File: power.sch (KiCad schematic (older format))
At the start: 33 parts, among them J2 4DB-P108-06, J3 39531-1002, J4 39531-1002, U2 i3A, U3 AP2112K-3.3TRG1

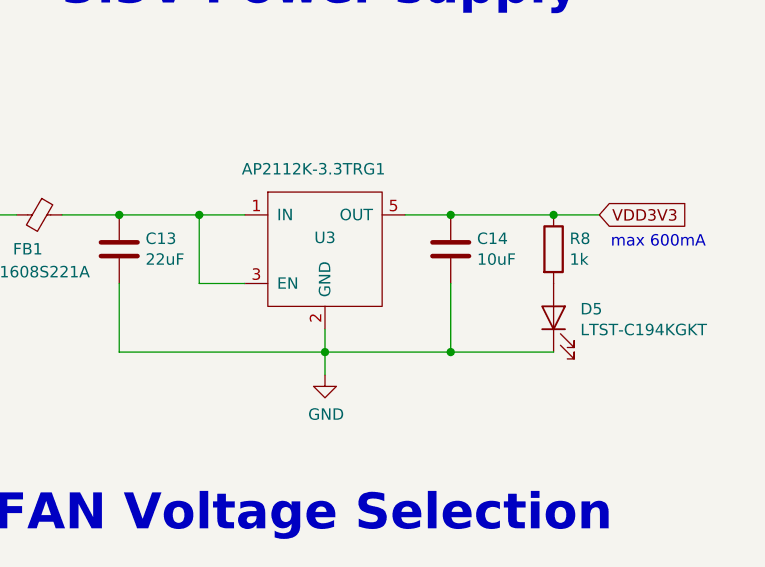
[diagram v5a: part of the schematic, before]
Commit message: Finish silkscreen and updated README.md
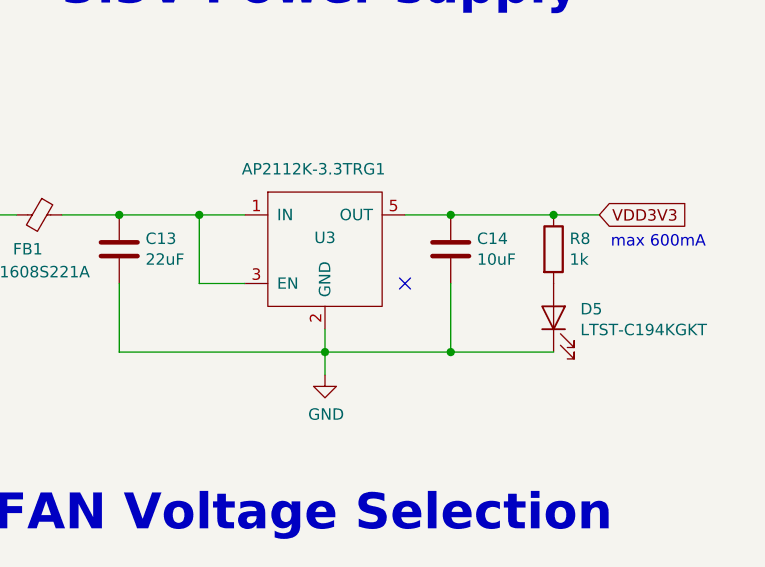
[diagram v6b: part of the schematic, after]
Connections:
- no-connect marks 1 -> 2
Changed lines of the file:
@@
 Connection ~ 2200 4400
 Wire Wire Line
-	1400 4000 2050 4000
-Wire Wire Line
 	2050 4000 2050 5600
-Wire Wire Line
-	2050 5600 2450 5600
 Wire Wire Line
 	2950 3800 3550 3800
@@
 Connection ~ 8450 1750
 Wire Wire Line
-	8450 1750 8900 1750
-Wire Wire Line
 	6750 1750 7000 1750
-Wire Wire Line
-	7000 1750 7350 1750
 Connection ~ 7000 1750
 Connection ~ 7350 1750
@@
 	3750 1450 3750 1250
 Connection ~ 3750 1250
+Connection ~ 2050 1250
+Wire Wire Line
+	2050 1250 2450 1250
+Wire Wire Line
+	1400 4000 2050 4000
+NoConn ~ 8250 2050
+Wire Wire Line
+	2050 5600 2450 5600
 Wire Wire Line
 	3750 1250 4550 1250
-Connection ~ 2050 1250
-Wire Wire Line
-	2050 1250 2450 1250
+Wire Wire Line
+	7000 1750 7350 1750
+Wire Wire Line
+	8450 1750 8900 1750
 $EndSCHEMATC

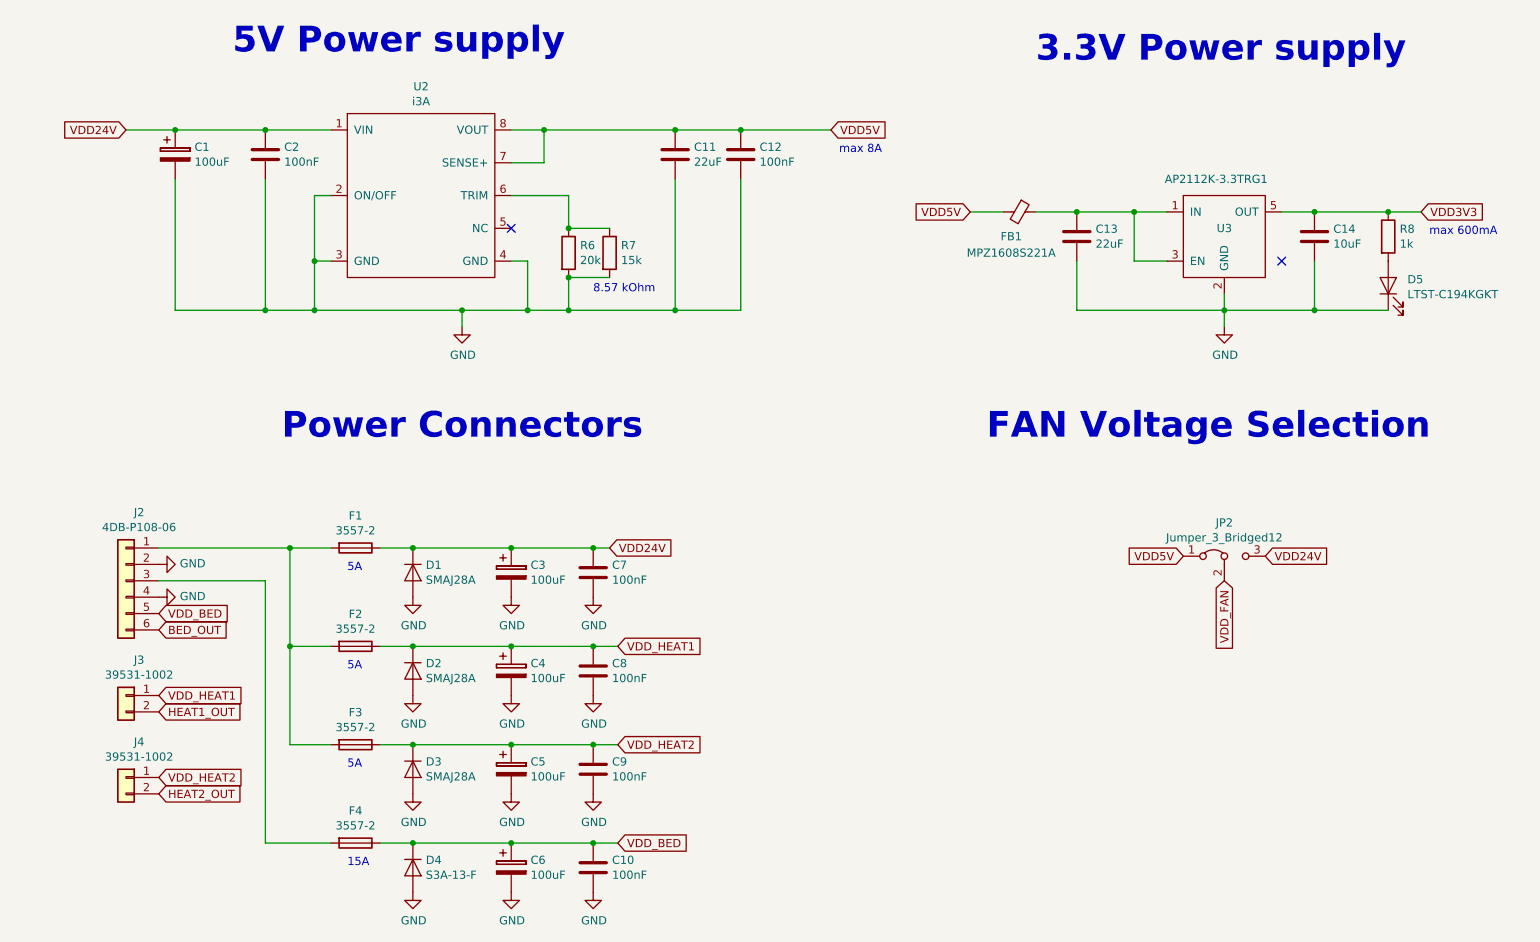
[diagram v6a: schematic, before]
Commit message: Add bypass cap for I2C EEPROMs and redone some copper pour
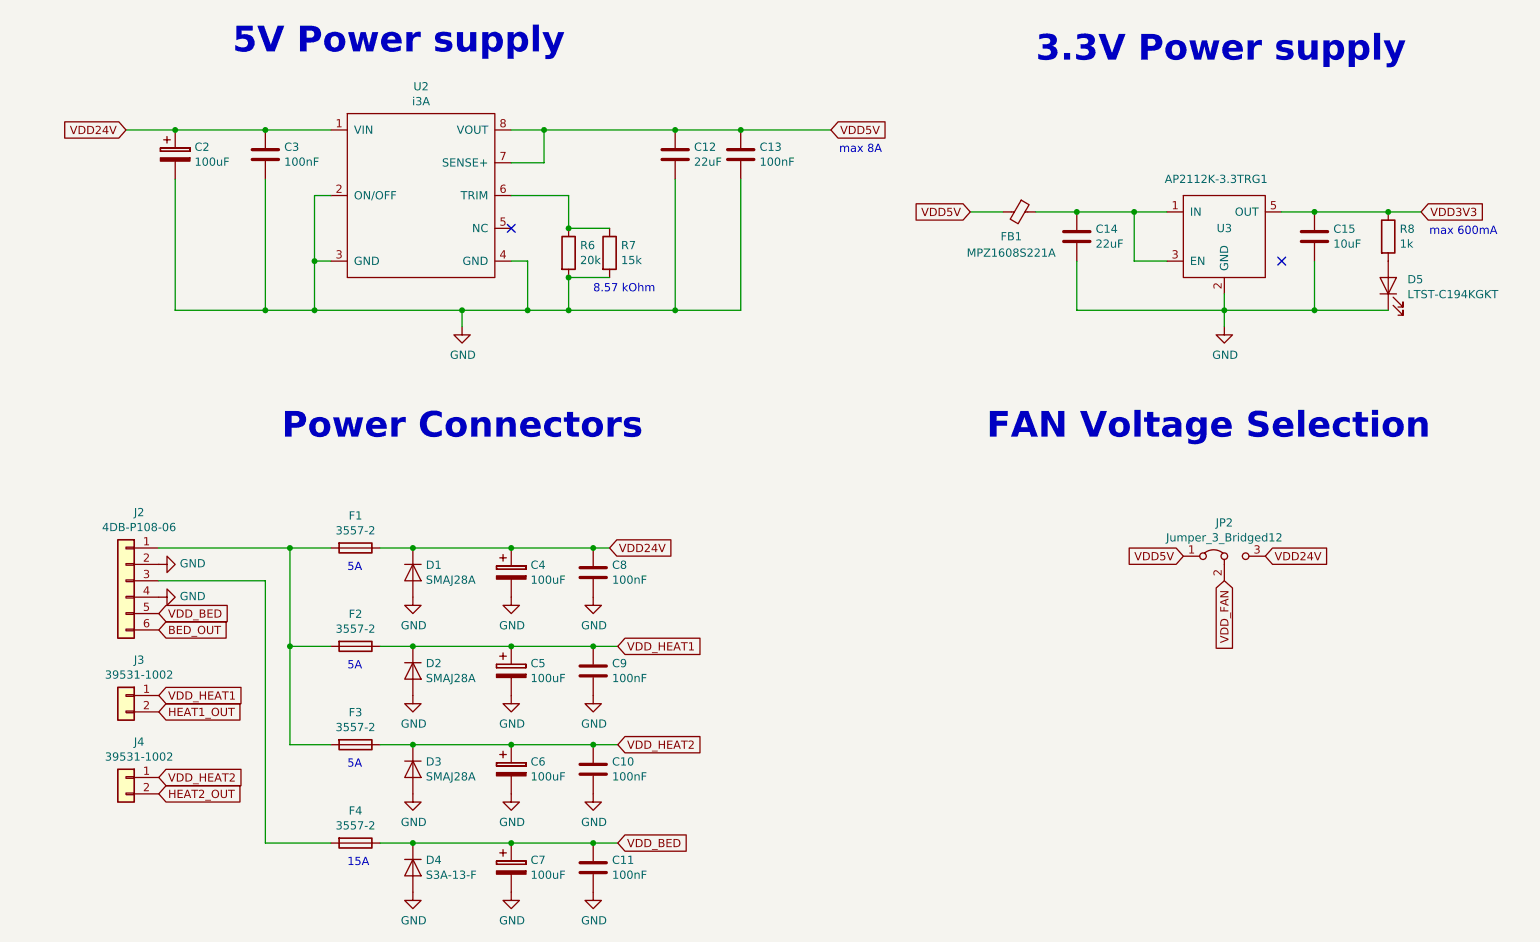
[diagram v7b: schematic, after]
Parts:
- renumbered C9 to C10, C10 to C11, C11 to C12, C12 to C13, C13 to C14, C14 to C15, C1 to C2, C2 to C3, C3 to C4, C4 to C5, C5 to C6, C6 to C7, C7 to C8, C8 to C9
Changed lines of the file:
@@
 $EndComp
 $Comp
-L power:GND #PWR020
+L power:GND #PWR021
 U 1 1 5BC561B5
 P 3250 2450
-F 0 "#PWR020" H 3250 2200 50  0001 C CNN
+F 0 "#PWR021" H 3250 2200 50  0001 C CNN
 F 1 "GND" H 3255 2277 50  0000 C CNN
 F 2 "" H 3250 2450 50  0001 C CNN
@@
 VDD5V
 $Comp
-L Device:C C11
+L Device:C C12
 U 1 1 5BC5651E
 P 4550 1400
-F 0 "C11" H 4665 1446 50  0000 L CNN
+F 0 "C12" H 4665 1446 50  0000 L CNN
 F 1 "22uF" H 4665 1355 50  0000 L CNN
 F 2 "Capacitor_SMD:C_1206_3216Metric" H 4588 1250 50  0001 C CNN
@@
 $EndComp
 $Comp
-L Device:CP C1
+L Device:CP C2
 U 1 1 5BC5695B
 P 1500 1400
-F 0 "C1" H 1618 1446 50  0000 L CNN
+F 0 "C2" H 1618 1446 50  0000 L CNN
 F 1 "100uF" H 1618 1355 50  0000 L CNN
 F 2 "Capacitor_SMD:CP_Elec_6.3x5.7" H 1538 1250 50  0001 C CNN
@@
 	7350 1750 7550 1750
 $Comp
-L power:GND #PWR029
+L power:GND #PWR030
 U 1 1 5BC5D77D
 P 7900 2450
-F 0 "#PWR029" H 7900 2200 50  0001 C CNN
+F 0 "#PWR030" H 7900 2200 50  0001 C CNN
 F 1 "GND" H 7905 2277 50  0000 C CNN
 F 2 "" H 7900 2450 50  0001 C CNN
@@
 5A
 $Comp
-L power:GND #PWR014
+L power:GND #PWR015
 U 1 1 5BC67A0E
 P 1400 3900
-F 0 "#PWR014" H 1400 3650 50  0001 C CNN
+F 0 "#PWR015" H 1400 3650 50  0001 C CNN
 F 1 "GND" V 1405 3772 50  0000 R CNN
 F 2 "" H 1400 3900 50  0001 C CNN
@@
 $EndComp
 $Comp
-L power:GND #PWR015
+L power:GND #PWR016
 U 1 1 5BC67AD5
 P 1400 4100
-F 0 "#PWR015" H 1400 3850 50  0001 C CNN
+F 0 "#PWR016" H 1400 3850 50  0001 C CNN
 F 1 "GND" V 1405 3972 50  0000 R CNN
 F 2 "" H 1400 4100 50  0001 C CNN
@@
 Connection ~ 2950 4400
 $Comp
-L Device:C C10
+L Device:C C11
 U 1 1 5BC33D64
 P 4050 5750
-F 0 "C10" H 4165 5796 50  0000 L CNN
+F 0 "C11" H 4165 5796 50  0000 L CNN
 F 1 "100nF" H 4165 5705 50  0000 L CNN
 F 2 "Capacitor_SMD:C_1812_4532Metric" H 4088 5600 50  0001 C CNN
@@
 Connection ~ 4050 5600
 $Comp
-L Device:C C8
+L Device:C C9
 U 1 1 5BC33D86
 P 4050 4550
-F 0 "C8" H 4165 4596 50  0000 L CNN
+F 0 "C9" H 4165 4596 50  0000 L CNN
 F 1 "100nF" H 4165 4505 50  0000 L CNN
 F 2 "Capacitor_SMD:C_1812_4532Metric" H 4088 4400 50  0001 C CNN
@@
 $EndComp
 $Comp
-L Device:C C7
+L Device:C C8
 U 1 1 5BC33D8D
 P 4050 3950
-F 0 "C7" H 4165 3996 50  0000 L CNN
+F 0 "C8" H 4165 3996 50  0000 L CNN
 F 1 "100nF" H 4165 3905 50  0000 L CNN
 F 2 "Capacitor_SMD:C_1812_4532Metric" H 4088 3800 50  0001 C CNN
@@
 Connection ~ 2950 5000
 $Comp
-L Device:C C9
+L Device:C C10
 U 1 1 5BC3EA40
 P 4050 5150
-F 0 "C9" H 4165 5196 50  0000 L CNN
+F 0 "C10" H 4165 5196 50  0000 L CNN
 F 1 "100nF" H 4165 5105 50  0000 L CNN
 F 2 "Capacitor_SMD:C_1812_4532Metric" H 4088 5000 50  0001 C CNN
@@
 	4050 5000 4200 5000
 $Comp
-L power:GND #PWR016
+L power:GND #PWR017
 U 1 1 5BC55678
 P 2950 4100
-F 0 "#PWR016" H 2950 3850 50  0001 C CNN
+F 0 "#PWR017" H 2950 3850 50  0001 C CNN
 F 1 "GND" H 2955 3927 50  0000 C CNN
 F 2 "" H 2950 4100 50  0001 C CNN
@@
 $EndComp
 $Comp
-L power:GND #PWR021
+L power:GND #PWR022
 U 1 1 5BC5572B
 P 3550 4100
-F 0 "#PWR021" H 3550 3850 50  0001 C CNN
+F 0 "#PWR022" H 3550 3850 50  0001 C CNN
 F 1 "GND" H 3555 3927 50  0000 C CNN
 F 2 "" H 3550 4100 50  0001 C CNN
@@
 $EndComp
 $Comp
-L power:GND #PWR025
+L power:GND #PWR026
 U 1 1 5BC56CA8
 P 4050 4100
-F 0 "#PWR025" H 4050 3850 50  0001 C CNN
+F 0 "#PWR026" H 4050 3850 50  0001 C CNN
 F 1 "GND" H 4055 3927 50  0000 C CNN
 F 2 "" H 4050 4100 50  0001 C CNN
@@
 $EndComp
 $Comp
-L power:GND #PWR026
+L power:GND #PWR027
 U 1 1 5BC581AF
 P 4050 4700
-F 0 "#PWR026" H 4050 4450 50  0001 C CNN
+F 0 "#PWR027" H 4050 4450 50  0001 C CNN
 F 1 "GND" H 4055 4527 50  0000 C CNN
 F 2 "" H 4050 4700 50  0001 C CNN
@@
 $EndComp
 $Comp
-L power:GND #PWR022
+L power:GND #PWR023
 U 1 1 5BC596B6
 P 3550 4700
-F 0 "#PWR022" H 3550 4450 50  0001 C CNN
+F 0 "#PWR023" H 3550 4450 50  0001 C CNN
 F 1 "GND" H 3555 4527 50  0000 C CNN
 F 2 "" H 3550 4700 50  0001 C CNN
@@
 $EndComp
 $Comp
-L power:GND #PWR017
+L power:GND #PWR018
 U 1 1 5BC5ABBD
 P 2950 4700
-F 0 "#PWR017" H 2950 4450 50  0001 C CNN
+F 0 "#PWR018" H 2950 4450 50  0001 C CNN
 F 1 "GND" H 2955 4527 50  0000 C CNN
 F 2 "" H 2950 4700 50  0001 C CNN
@@
 $EndComp
 $Comp
-L power:GND #PWR018
+L power:GND #PWR019
 U 1 1 5BC5C0C4
 P 2950 5300
-F 0 "#PWR018" H 2950 5050 50  0001 C CNN
+F 0 "#PWR019" H 2950 5050 50  0001 C CNN
 F 1 "GND" H 2955 5127 50  0000 C CNN
 F 2 "" H 2950 5300 50  0001 C CNN
@@
 $EndComp
 $Comp
-L power:GND #PWR023
+L power:GND #PWR024
 U 1 1 5BC5D5CB
 P 3550 5300
-F 0 "#PWR023" H 3550 5050 50  0001 C CNN
+F 0 "#PWR024" H 3550 5050 50  0001 C CNN
 F 1 "GND" H 3555 5127 50  0000 C CNN
 F 2 "" H 3550 5300 50  0001 C CNN
@@
 $EndComp
 $Comp
-L power:GND #PWR027
+L power:GND #PWR028
 U 1 1 5BC5EAD2
 P 4050 5300
-F 0 "#PWR027" H 4050 5050 50  0001 C CNN
+F 0 "#PWR028" H 4050 5050 50  0001 C CNN
 F 1 "GND" H 4055 5127 50  0000 C CNN
 F 2 "" H 4050 5300 50  0001 C CNN
@@
 $EndComp
 $Comp
-L power:GND #PWR019
+L power:GND #PWR020
 U 1 1 5BC6011D
 P 2950 5900
-F 0 "#PWR019" H 2950 5650 50  0001 C CNN
+F 0 "#PWR020" H 2950 5650 50  0001 C CNN
 F 1 "GND" H 2955 5727 50  0000 C CNN
 F 2 "" H 2950 5900 50  0001 C CNN
@@
 $EndComp
 $Comp
-L power:GND #PWR024
+L power:GND #PWR025
 U 1 1 5BC61624
 P 3550 5900
-F 0 "#PWR024" H 3550 5650 50  0001 C CNN
+F 0 "#PWR025" H 3550 5650 50  0001 C CNN
 F 1 "GND" H 3555 5727 50  0000 C CNN
 F 2 "" H 3550 5900 50  0001 C CNN
@@
 $EndComp
 $Comp
-L power:GND #PWR028
+L power:GND #PWR029
 U 1 1 5BC62B2B
 P 4050 5900
-F 0 "#PWR028" H 4050 5650 50  0001 C CNN
+F 0 "#PWR029" H 4050 5650 50  0001 C CNN
 F 1 "GND" H 4055 5727 50  0000 C CNN
 F 2 "" H 4050 5900 50  0001 C CNN
@@
 	2950 5600 3550 5600
 $Comp
-L Device:CP C5
+L Device:CP C6
 U 1 1 5BC4FDD0
 P 3550 5150
-F 0 "C5" H 3668 5196 50  0000 L CNN
+F 0 "C6" H 3668 5196 50  0000 L CNN
 F 1 "100uF" H 3668 5105 50  0000 L CNN
 F 2 "Capacitor_SMD:CP_Elec_6.3x5.7" H 3588 5000 50  0001 C CNN
@@
 $EndComp
 $Comp
-L Device:CP C4
+L Device:CP C5
 U 1 1 5BC51306
 P 3550 4550
-F 0 "C4" H 3668 4596 50  0000 L CNN
+F 0 "C5" H 3668 4596 50  0000 L CNN
 F 1 "100uF" H 3668 4505 50  0000 L CNN
 F 2 "Capacitor_SMD:CP_Elec_6.3x5.7" H 3588 4400 50  0001 C CNN
@@
 $EndComp
 $Comp
-L Device:CP C3
+L Device:CP C4
 U 1 1 5BC52840
 P 3550 3950
-F 0 "C3" H 3668 3996 50  0000 L CNN
+F 0 "C4" H 3668 3996 50  0000 L CNN
 F 1 "100uF" H 3668 3905 50  0000 L CNN
 F 2 "Capacitor_SMD:CP_Elec_6.3x5.7" H 3588 3800 50  0001 C CNN
@@
 $EndComp
 $Comp
-L Device:CP C6
+L Device:CP C7
 U 1 1 5BC53D94
 P 3550 5750
-F 0 "C6" H 3668 5796 50  0000 L CNN
+F 0 "C7" H 3668 5796 50  0000 L CNN
 F 1 "100uF" H 3668 5705 50  0000 L CNN
 F 2 "Capacitor_SMD:CP_Elec_6.3x5.7" H 3588 5600 50  0001 C CNN
@@
 	3550 3800 4050 3800
 $Comp
-L Device:C C13
+L Device:C C14
 U 1 1 5BCBCE1D
 P 7000 1900
-F 0 "C13" H 7115 1946 50  0000 L CNN
+F 0 "C14" H 7115 1946 50  0000 L CNN
 F 1 "22uF" H 7115 1855 50  0000 L CNN
 F 2 "Capacitor_SMD:C_1206_3216Metric" H 7038 1750 50  0001 C CNN
@@
 	6350 1750 6550 1750
 $Comp
-L Device:C C14
+L Device:C C15
 U 1 1 5BCCA55E
 P 8450 1900
-F 0 "C14" H 8565 1946 50  0000 L CNN
+F 0 "C15" H 8565 1946 50  0000 L CNN
 F 1 "10uF" H 8565 1855 50  0000 L CNN
 F 2 "Capacitor_SMD:C_1206_3216Metric" H 8488 1750 50  0001 C CNN
@@
 FAN Voltage Selection
 $Comp
-L Device:C C12
+L Device:C C13
 U 1 1 5BC565B1
 P 4950 1400
-F 0 "C12" H 5065 1446 50  0000 L CNN
+F 0 "C13" H 5065 1446 50  0000 L CNN
 F 1 "100nF" H 5065 1355 50  0000 L CNN
 F 2 "Capacitor_SMD:C_1206_3216Metric" H 4988 1250 50  0001 C CNN
@@
 Connection ~ 2350 2050
 $Comp
-L Device:C C2
+L Device:C C3
 U 1 1 5BCFC548
 P 2050 1400
-F 0 "C2" H 2165 1446 50  0000 L CNN
+F 0 "C3" H 2165 1446 50  0000 L CNN
 F 1 "100nF" H 2165 1355 50  0000 L CNN
 F 2 "Capacitor_SMD:C_1812_4532Metric" H 2088 1250 50  0001 C CNN

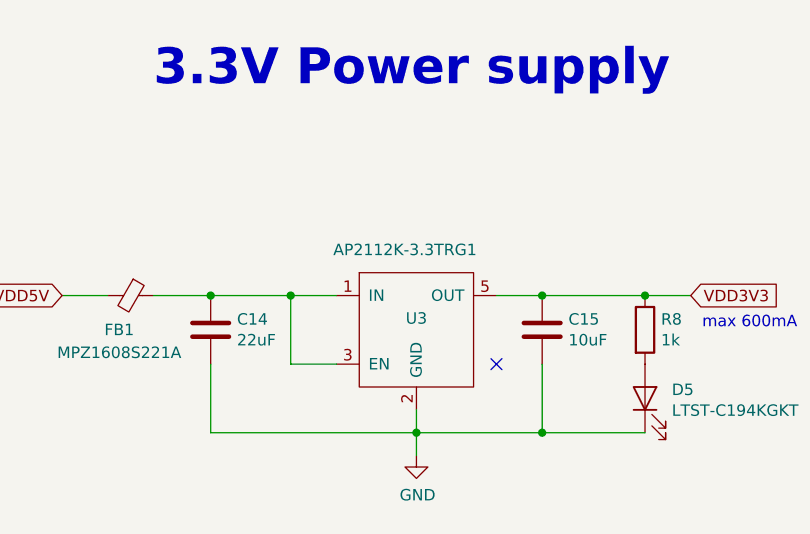
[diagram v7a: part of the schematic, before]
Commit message: Fix various v1.0 errors
 * Change 3.3V LDO to AP7365-33WG-7
 * Optimize soldermask clearance (from 0.2 to 0.05)
 * Connect SD connect switch to GND
 * Optimized some PADs
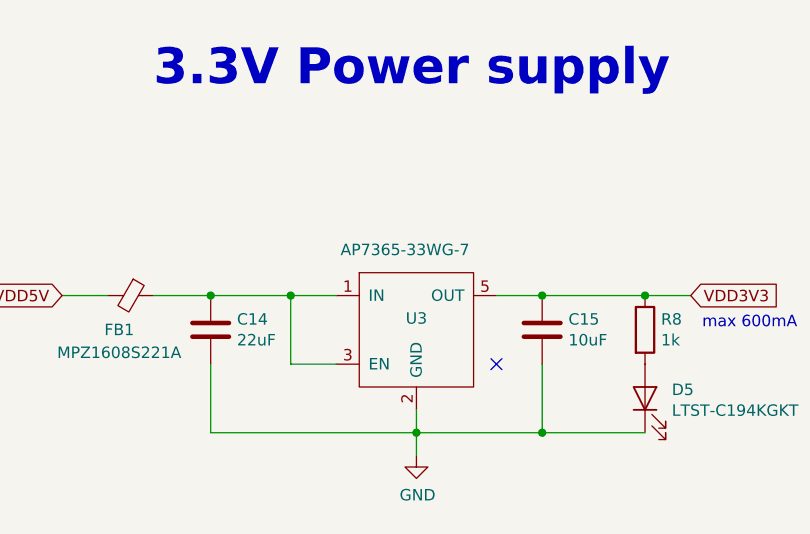
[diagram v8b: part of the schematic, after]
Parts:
- U3: value AP2112K-3.3TRG1 -> AP7365-33WG-7
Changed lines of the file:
@@
 P 7900 1850
 F 0 "U3" H 7900 1850 50  0000 C CNN
-F 1 "AP2112K-3.3TRG1" H 7850 2150 50  0000 C CNN
+F 1 "AP7365-33WG-7" H 7850 2150 50  0000 C CNN
 F 2 "Package_TO_SOT_SMD:SOT-23-5" H 7900 1850 50  0001 C CNN
-F 3 "https://www.diodes.com/assets/Datasheets/AP2112.pdf" H 7900 1850 50  0001 C CNN
+F 3 "https://www.mouser.de/datasheet/2/115/AP7365-86154.pdf" H 7900 1850 50  0001 C CNN
 	1    7900 1850
 	1    0    0    -1
